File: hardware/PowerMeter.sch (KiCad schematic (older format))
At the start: 42 parts, among them P1 CONN_1, P10 CONN_1, P2 CONN_1, P3 CONN_1, P4 CONN_1, P5 CONN_1, P6 CONN_1, P7 CONN_1, P8 CONN_5, P9 CONN_1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

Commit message: Move some text labels, add to-do notes to board and schematic
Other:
- note added: "To do:\nmove battery voltage ADC input after diode\n (protect MCU against reverse polarity)"
- note removed: "To do:\ndone: add probe pins\ndone: add extra pins on unused ports\ndone: add diode on batt+"
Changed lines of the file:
@@
-EESchema Schematic File Version 2  date Sun 02 Oct 2011 14:36:11 BST
+EESchema Schematic File Version 2  date Wed 05 Oct 2011 09:01:31 BST
 LIBS:dresco
 LIBS:PowerMeter-cache
@@
 Sheet 1 1
 Title ""
-Date "2 oct 2011"
+Date "5 oct 2011"
 Rev "0.3"
 Comp ""
@@
 $EndComp
 Text Notes 700  6950 0    120  ~ 0
-To do:\ndone: add probe pins\ndone: add extra pins on unused ports\ndone: add diode on batt+
+To do:\nmove battery voltage ADC input after diode\n (protect MCU against reverse polarity)
 NoConn ~ 6800 5100
 NoConn ~ 6800 5000

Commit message: Move batt+ ADC input after diode, move XBee module within board outline
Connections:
- net +BATT: no longer R2.1
- net VI: now reaches C1.1, D1.2 (K), U1.VI
- net VI: now also R2.1
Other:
- note added: "To do:\n..."
- note removed: "To do:\nmove battery voltage ADC input after diode\n (protect MCU against reverse polarity)"

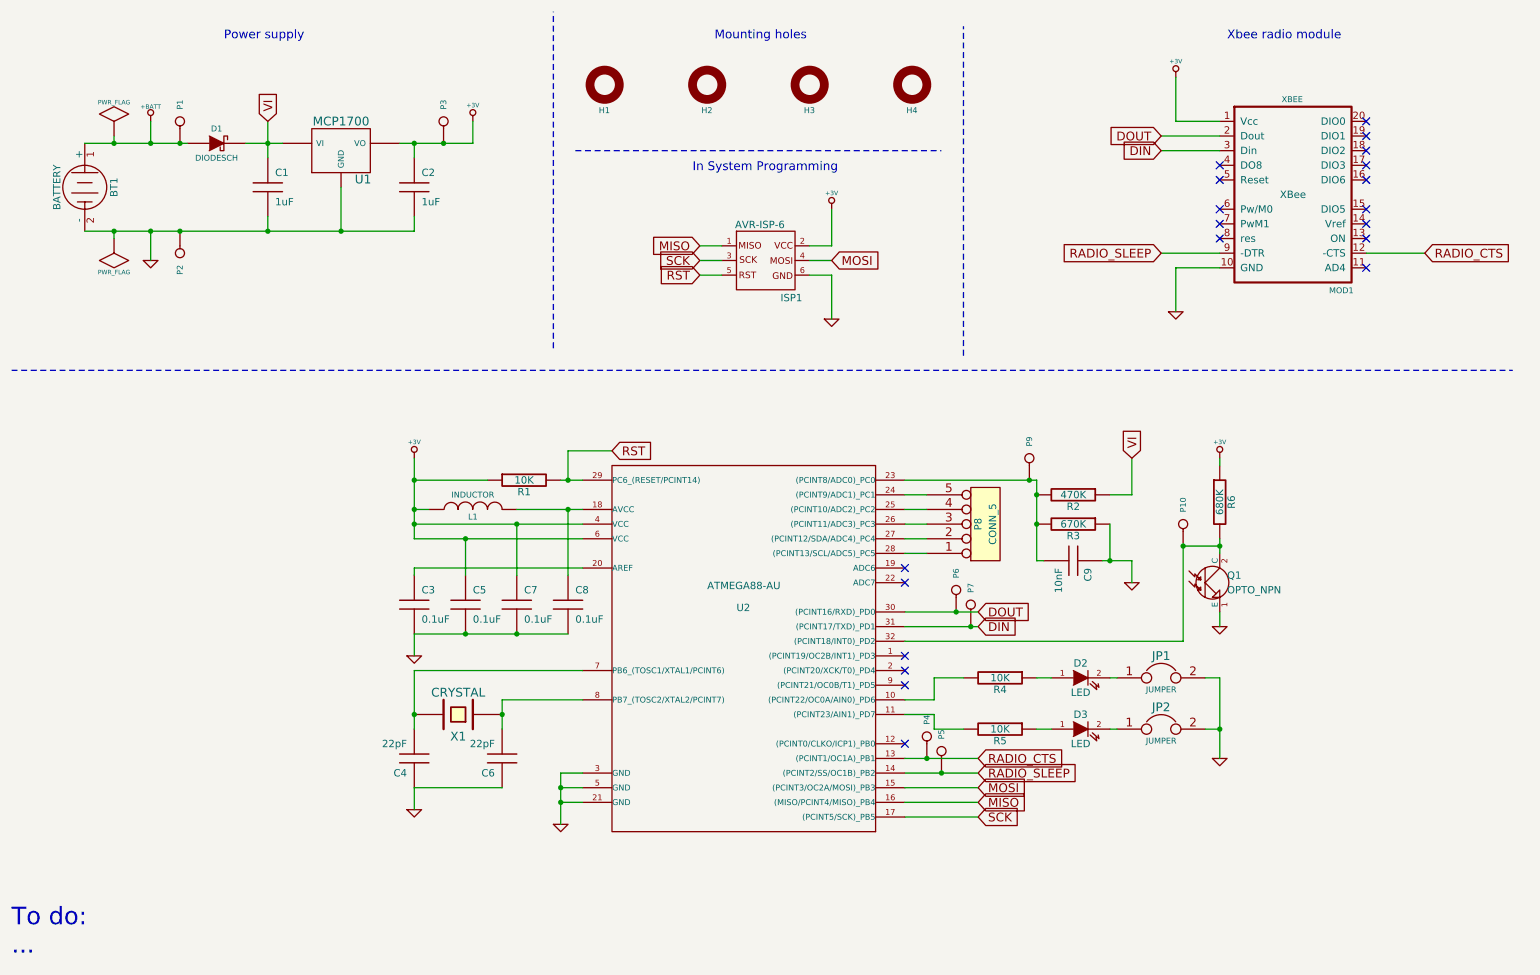
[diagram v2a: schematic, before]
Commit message: Add new test point for VIN, use one via for both XTAL caps
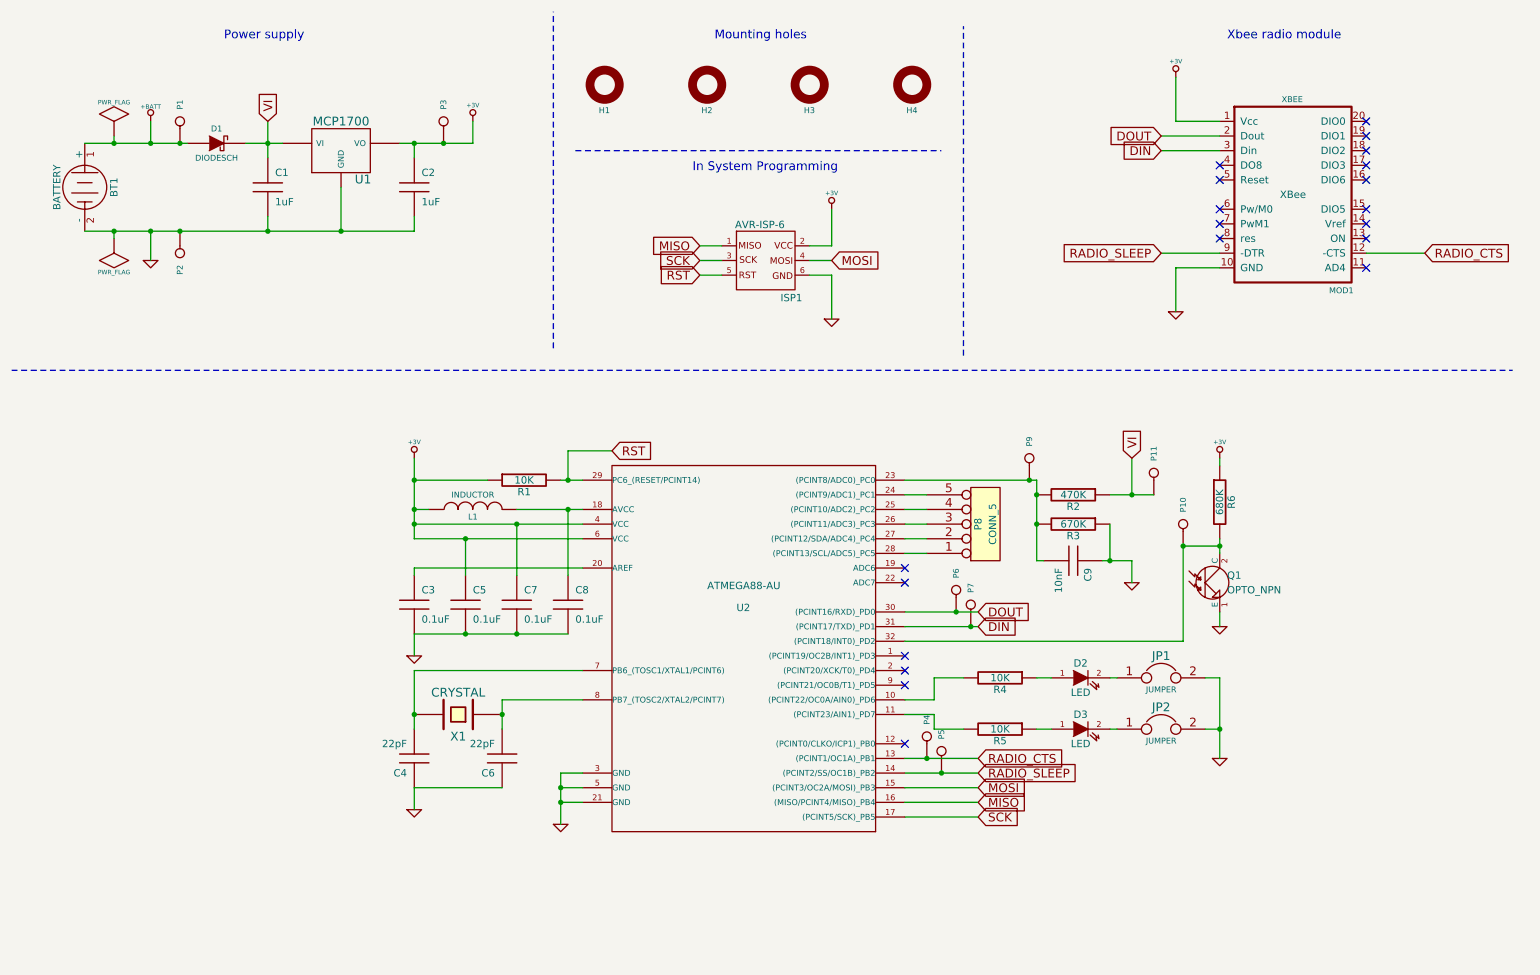
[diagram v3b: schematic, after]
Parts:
- added P11: CONN_1, symbol CONN_1
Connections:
- net VI: now also P11.1
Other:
- note removed: "To do:\n..."

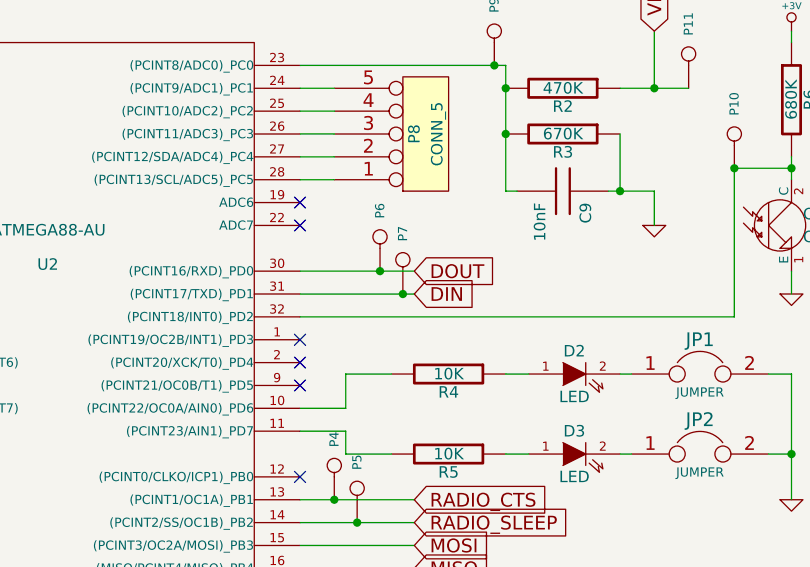
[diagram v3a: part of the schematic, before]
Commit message: Add new test point for INT1
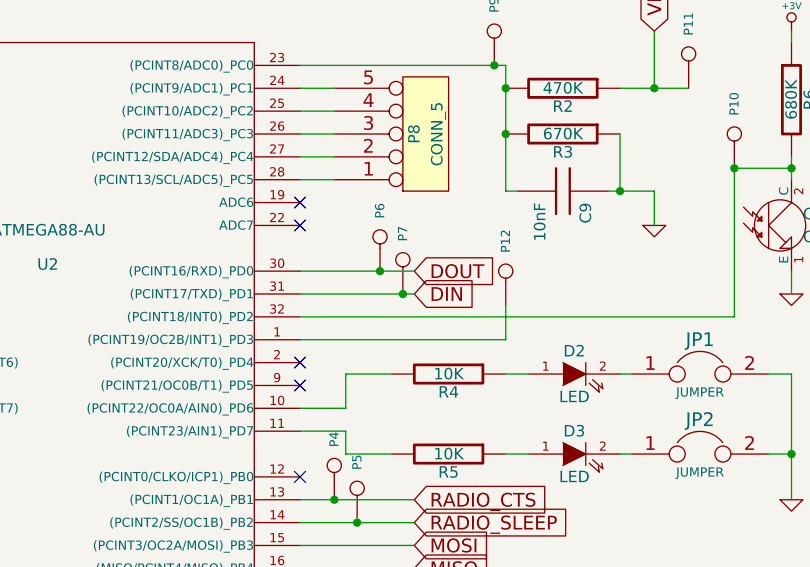
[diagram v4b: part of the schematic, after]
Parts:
- added P12: CONN_1, symbol CONN_1
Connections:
- net at U2.1 ((PCINT19/OC2B/INT1)_PD3): now also P12.1
- no-connect marks 20 -> 19
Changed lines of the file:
@@
-EESchema Schematic File Version 2  date Sat 08 Oct 2011 21:36:08 BST
+EESchema Schematic File Version 2  date Sat 08 Oct 2011 21:52:02 BST
 LIBS:dresco
 LIBS:PowerMeter-cache
@@
 Comment4 ""
 $EndDescr
+Wire Wire Line
+	7700 4750 7700 4900
 Connection ~ 8350 3800
 Wire Wire Line
@@
 Wire Wire Line
 	2450 1250 2450 1500
+Wire Wire Line
+	7700 4900 6800 4900
+$Comp
+L CONN_1 P12
+U 1 1 4E90B79C
+P 7700 4600
+F 0 "P12" H 7780 4600 40  0000 L CNN
+F 1 "CONN_1" H 7700 4655 30  0001 C CNN
+	1    7700 4600
+	0    -1   -1   0
+$EndComp
 $Comp
 L CONN_1 P11
@@
 NoConn ~ 6800 5100
 NoConn ~ 6800 5000
-NoConn ~ 6800 4900
 NoConn ~ 6800 4400
 NoConn ~ 6800 4300
